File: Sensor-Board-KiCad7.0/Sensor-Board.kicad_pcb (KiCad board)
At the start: 2 copper layers, 75.4 x 75.4 mm, 128 parts, among them J2 B04B-XASK-1, U1 OPA396DCKT, U10 BME680, U11 OPA396DCKT, U12 OPA396DCKT, U14 OPA396DCKT, U15 MMBFJ177LT1, U16 MMBFJ177LT1, U17 MMBFJ177LT1, U18 NAU7802SGI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

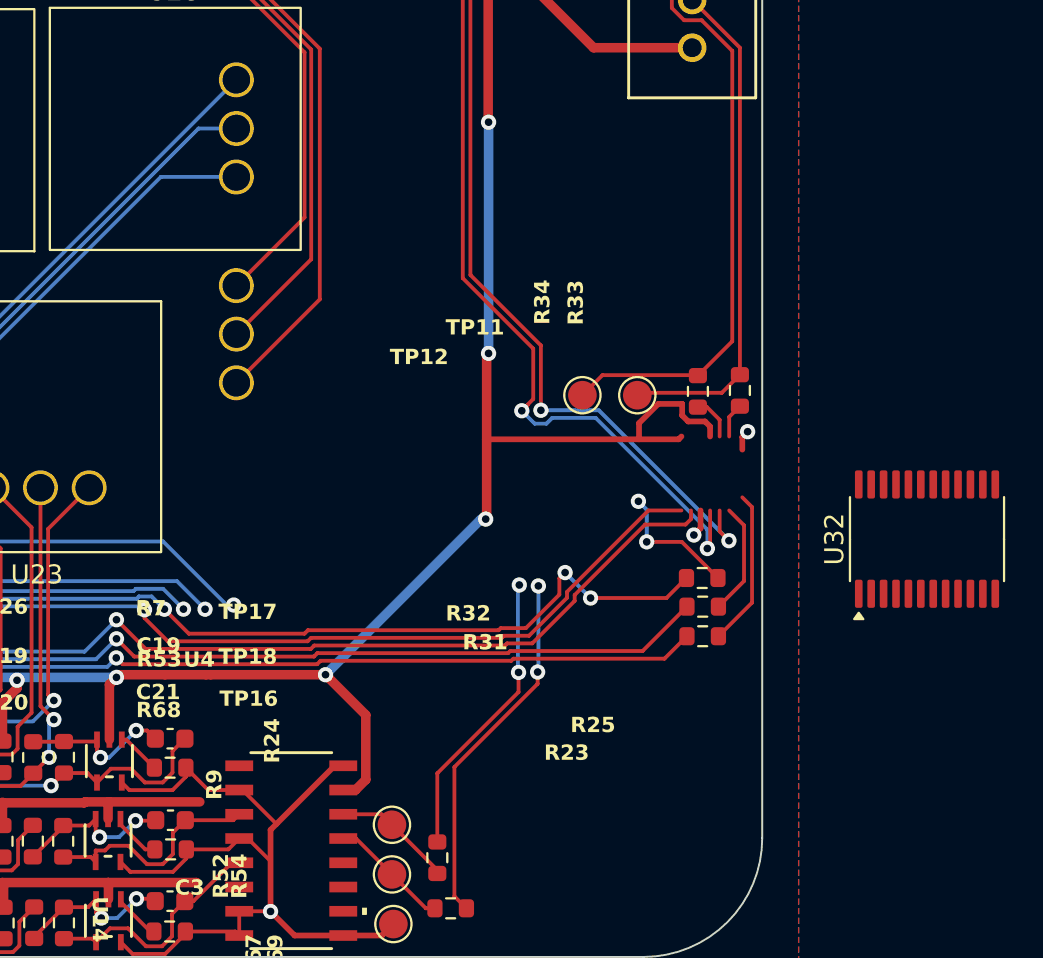
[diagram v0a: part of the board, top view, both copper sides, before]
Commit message: Moved resistors and wired the last of it all up
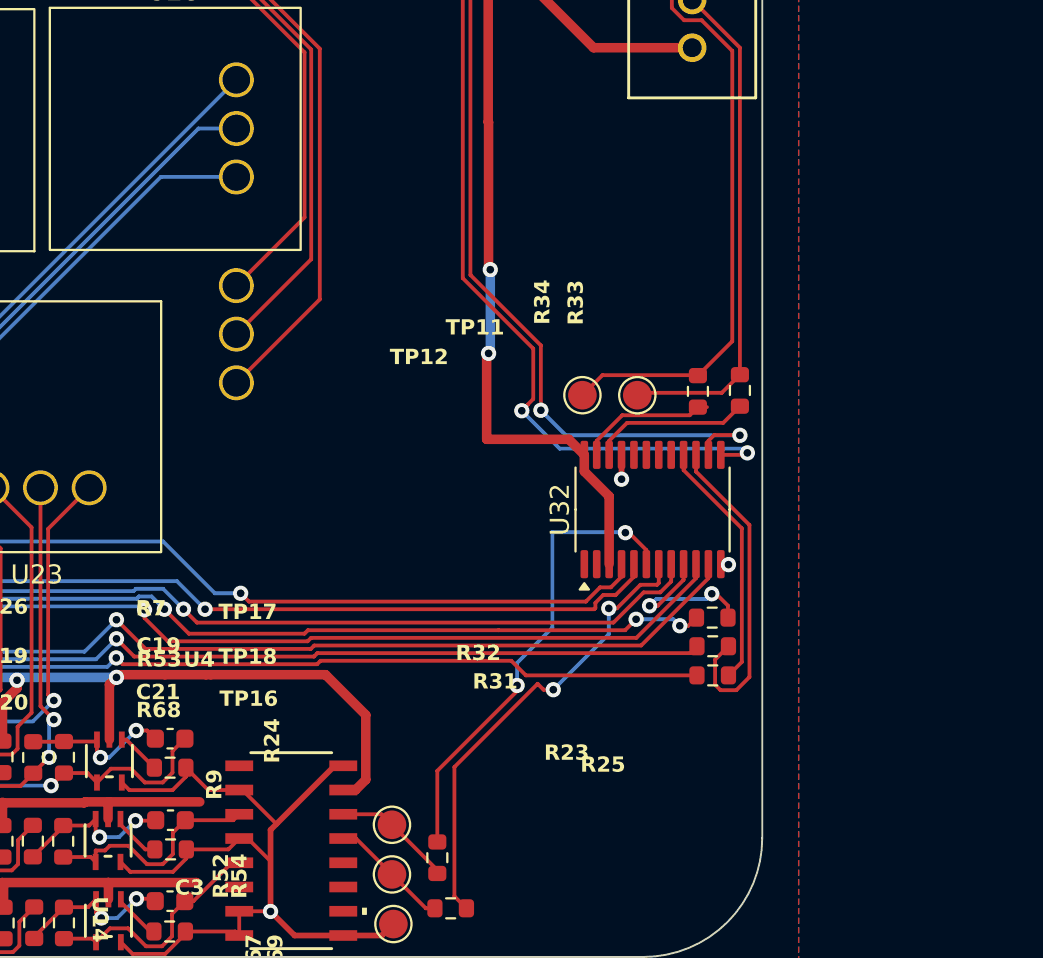
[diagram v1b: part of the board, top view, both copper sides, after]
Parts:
- moved U32 14.5 mm to (169.7, 109.9)
- moved R25 2.14 mm to (172.8, 115.5)
- moved R32 2.14 mm to (172.8, 117.0)
- moved R31 2.12 mm to (172.8, 118.6)
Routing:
- net Net-(U32-SD2): track 59.8 -> 87.4 mm
- net Net-(U32-SC0): track 59.2 -> 83.2 mm
- net Net-(U32-SD0): track 55.4 -> 76.8 mm
- net +3.3V: track 482.2 -> 461.4 mm, vias 15 -> 13
- net Net-(U32-SD5): track 5.91 -> 17.3 mm
- net Net-(U32-SD1): track 15.3 -> 24.8 mm
- net Net-(U32-SCL): track 1.82 -> 8.34 mm
- net Net-(U32-SC1): track 19.0 -> 24.4 mm
- net Net-(U32-SDA): track 2.29 -> 7.24 mm
- net Net-(U32-SC5): track 8.22 -> 13.1 mm
- net 680_SCL1: track 134.1 -> 132.4 mm
- net Net-(U32-SC2): track 6.82 -> 8.42 mm
- net Net-(U32-SC4): track 59.3 -> 58.3 mm
- net Net-(U32-SD4): track 61.2 -> 60.2 mm
- net GND: track 150.6 -> 149.8 mm

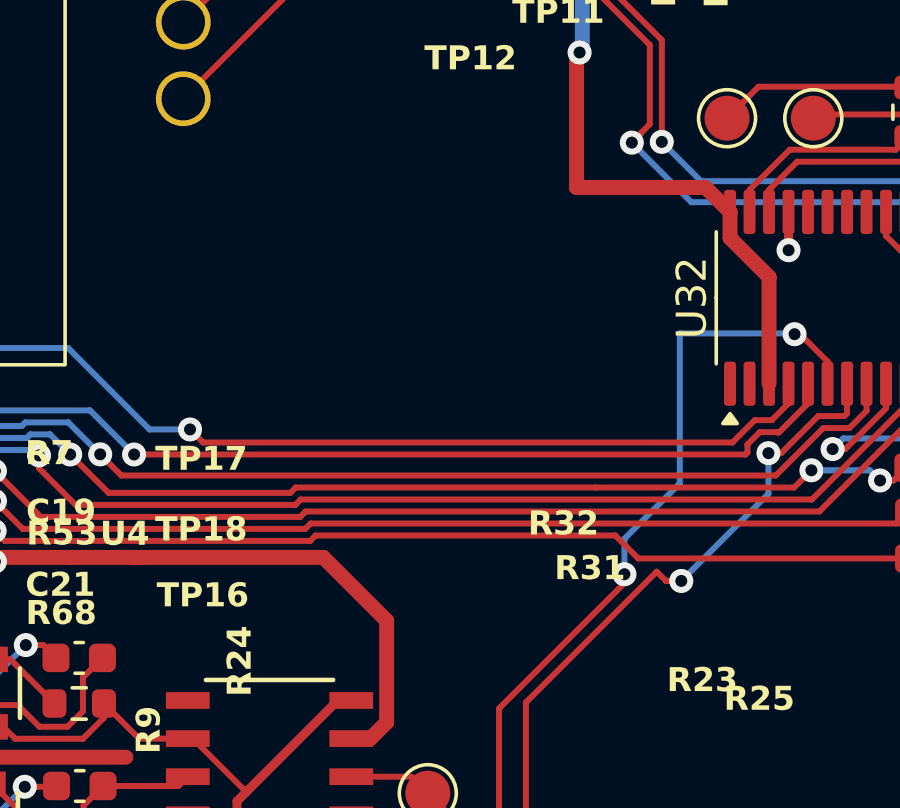
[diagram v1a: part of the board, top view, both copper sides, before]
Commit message: Rewired 3.3V to source line
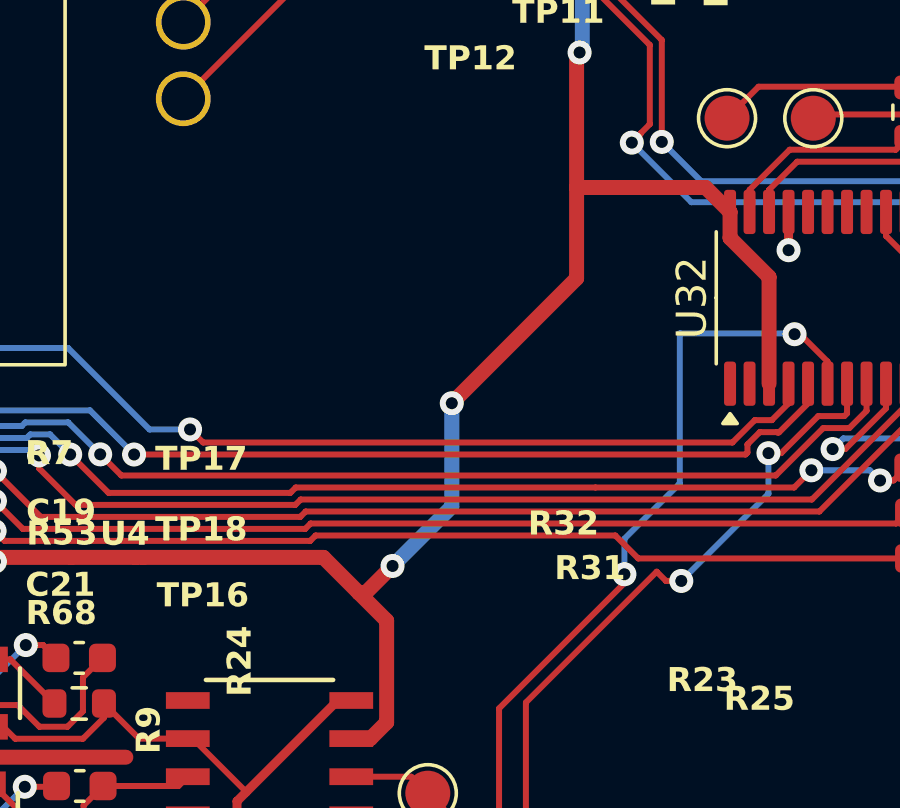
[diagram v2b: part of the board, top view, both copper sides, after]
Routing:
- net +3.3V: track 461.4 -> 478.1 mm, vias 13 -> 15
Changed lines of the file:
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@@
   (segment (start 122.32 100.772284) (end 121.845216 100.2975) (width 0.3) (layer "F.Cu") (net 9))
   (segment (start 122.649986 61.743336) (end 122.67 61.76335) (width 0.5) (layer "F.Cu") (net 9))
+  (segment (start 154.62855 120.64855) (end 153.7025 119.7225) (width 0.5) (layer "F.Cu") (net 9))
+  (segment (start 160.96 109.24) (end 156.8 113.4) (width 0.5) (layer "F.Cu") (net 9))
   (segment (start 122.77 65.84) (end 122.75 65.82) (width 0.5) (layer "F.Cu") (net 9))
   (segment (start 135.6 120.009188) (end 136.36 119.249188) (width 0.5) (layer "F.Cu") (net 9))
@@
   (segment (start 114.49 107.68) (end 114.49 105.52) (width 0.5) (layer "F.Cu") (net 9))
   (segment (start 103.92 81.85) (end 103.92 81.21035) (width 0.5) (layer "F.Cu") (net 9))
+  (segment (start 154.825 118.825) (end 153.9275 119.7225) (width 0.5) (layer "F.Cu") (net 9))
   (segment (start 136.36 119.249188) (end 136.36 118.83) (width 0.5) (layer "F.Cu") (net 9))
   (segment (start 103.92 84.062182) (end 103.682182 84.3) (width 0.5) (layer "F.Cu") (net 9))
@@
   (segment (start 154.08795 124.58) (end 154.62855 124.0394) (width 0.5) (layer "F.Cu") (net 9))
   (segment (start 117.28 123.37) (end 121.98 118.67) (width 0.5) (layer "F.Cu") (net 9))
+  (segment (start 153.9275 119.7225) (end 153.7025 119.7225) (width 0.5) (layer "F.Cu") (net 9))
   (segment (start 146.38 69.26) (end 146.38 71.6) (width 0.5) (layer "F.Cu") (net 9))
   (segment (start 120.71978 129.98) (end 117.44 129.98) (width 0.5) (layer "F.Cu") (net 9))
@@
   (segment (start 122.630001 129.356651) (end 122.630001 128.4979) (width 0.5) (layer "F.Cu") (net 9))
   (segment (start 111.20035 107.68) (end 114.49 107.68) (width 0.5) (layer "F.Cu") (net 9))
+  (segment (start 153.7025 119.7225) (end 152.52 118.54) (width 0.5) (layer "F.Cu") (net 9))
   (segment (start 116.51 70.1) (end 122.40545 70.1) (width 0.5) (layer "F.Cu") (net 9))
   (segment (start 135.55 65.78) (end 135.61 65.78) (width 0.5) (layer "F.Cu") (net 9))
@@
   (segment (start 120.72 100.91) (end 115.75 100.91) (width 0.3) (layer "F.Cu") (net 9))
   (segment (start 160.96 101.81) (end 160.96 106.21) (width 0.5) (layer "F.Cu") (net 9))
-  (segment (start 154.62855 120.64855) (end 152.52 118.54) (width 0.5) (layer "F.Cu") (net 9))
   (segment (start 161.06 89.6) (end 161.06 97.235) (width 0.5) (layer "F.Cu") (net 9))
   (segment (start 108.65 110.828668) (end 108.998418 110.48025) (width 0.5) (layer "F.Cu") (net 9))
   (segment (start 114.34 110.14) (end 114.49 109.99) (width 0.5) (layer "F.Cu") (net 9))
   (segment (start 121.52 100.2775) (end 121.5 100.2975) (width 0.3) (layer "F.Cu") (net 9))
+  (segment (start 160.96 106.21) (end 160.96 109.24) (width 0.5) (layer "F.Cu") (net 9))
   (segment (start 122.649986 60.8879) (end 122.649986 61.743336) (width 0.5) (layer "F.Cu") (net 9))
   (segment (start 102.925 100.35) (end 112.61 100.35) (width 0.5) (layer "F.Cu") (net 9))
@@
   (via (at 114.35 80.38) (size 0.8) (drill 0.4) (layers "F.Cu" "B.Cu") (net 9))
   (via (at 161.225 80.365) (size 0.8) (drill 0.4) (layers "F.Cu" "B.Cu") (net 9))
+  (via (at 156.8 113.4) (size 0.8) (drill 0.4) (layers "F.Cu" "B.Cu") (net 9))
+  (via (at 154.825 118.825) (size 0.8) (drill 0.4) (layers "F.Cu" "B.Cu") (net 9))
   (via (at 136.36 118.83) (size 0.8) (drill 0.4) (layers "F.Cu" "B.Cu") (net 9))
   (via (at 161.06 101.71) (size 0.8) (drill 0.4) (layers "F.Cu" "B.Cu") (net 9))
@@
   (segment (start 122.21 93.3) (end 122.21 91.65) (width 0.3) (layer "B.Cu") (net 9))
   (segment (start 114.34 111.03) (end 121.98 118.67) (width 0.5) (layer "B.Cu") (net 9))
+  (segment (start 156.8 113.4) (end 156.8 116.85) (width 0.5) (layer "B.Cu") (net 9))
+  (segment (start 156.8 116.85) (end 154.825 118.825) (width 0.5) (layer "B.Cu") (net 9))
   (segment (start 122.17 72.5) (end 122.17 72.43) (width 0.5) (layer "B.Cu") (net 9))
   (segment (start 122.647499 93.4) (end 122.31 93.4) (width 0.3) (layer "B.Cu") (net 9))

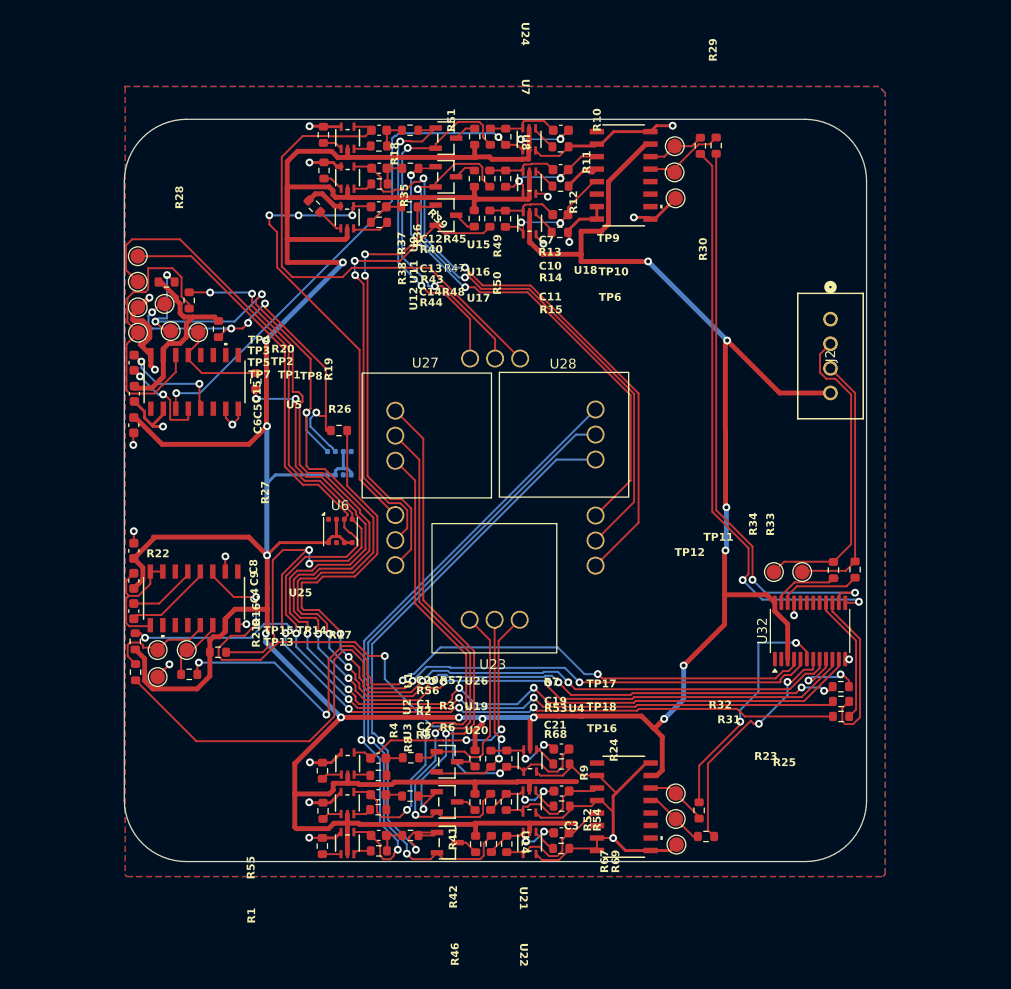
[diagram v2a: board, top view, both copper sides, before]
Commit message: Ordered silk screen stuff around circuit and wired up some unwired grnds
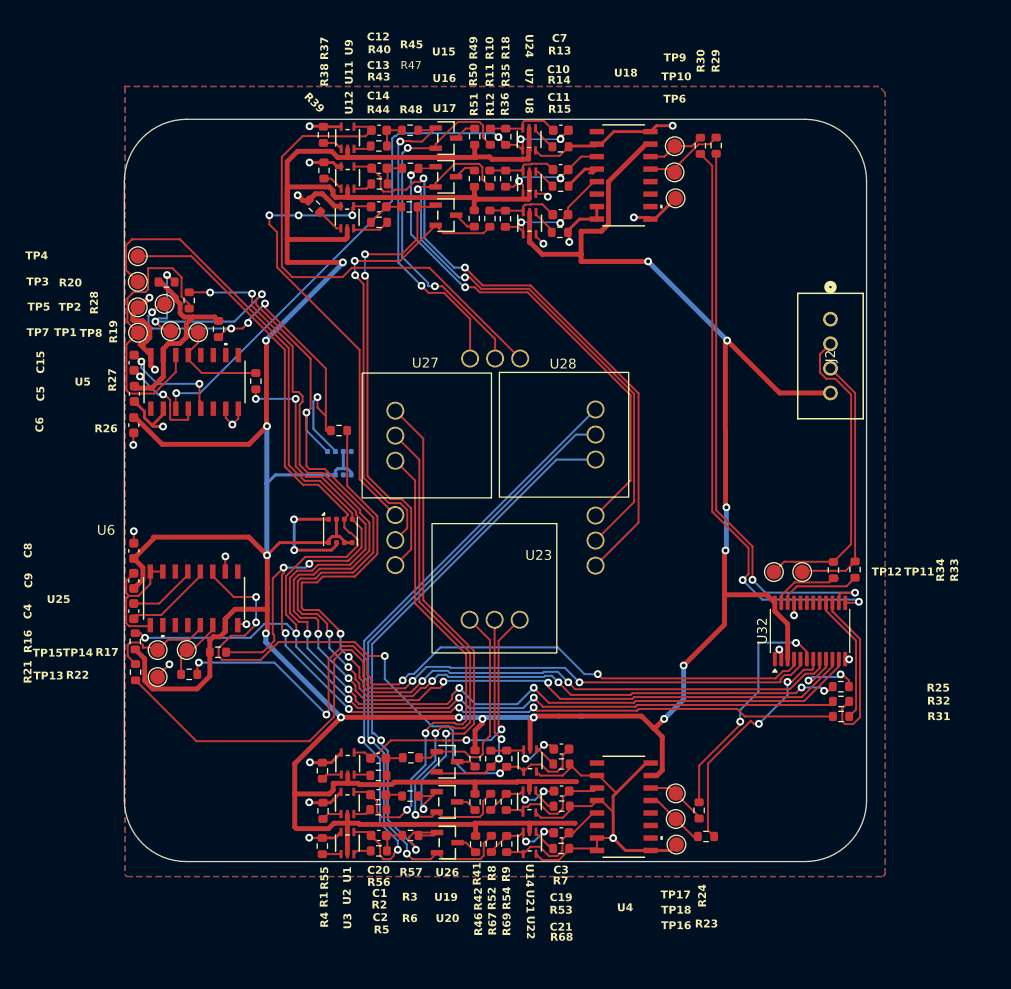
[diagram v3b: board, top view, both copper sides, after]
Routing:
- net GND: track 149.8 -> 163.6 mm, vias 22 -> 26
- net 680_SCL2: track 145.8 -> 139.8 mm
- net 680_SDA1: track 40.3 -> 42.8 mm

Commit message: Updated board edge clearance settings
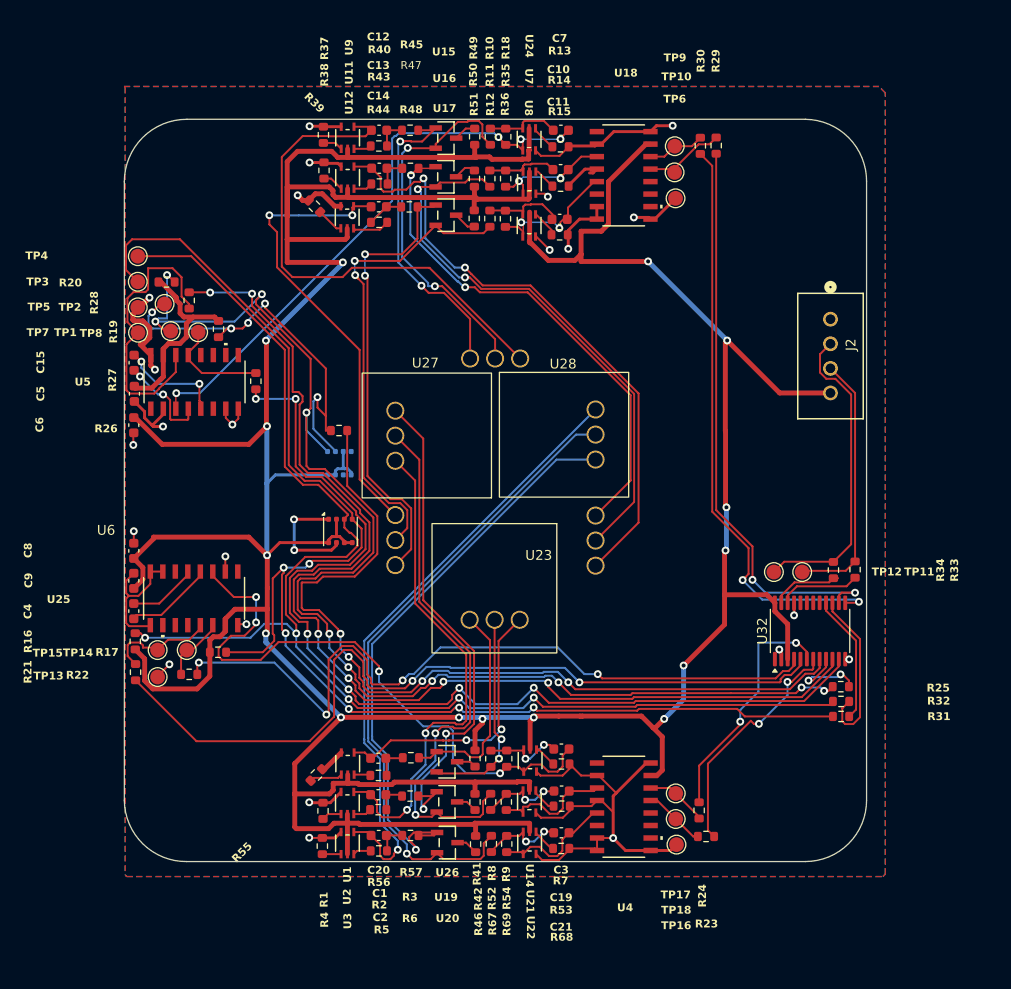
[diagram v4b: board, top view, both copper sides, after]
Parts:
- moved R55 0.75 mm to (119.5, 124.5), turned to 45 degrees
- moved C11 0.48 mm to (144.2, 68.0)
- moved R15 0.25 mm to (144.2, 69.6)
- moved U8 0.24 mm to (141.1, 68.7)
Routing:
- net +3.3V: track 478.1 -> 469.1 mm
- net Sens2_CO: track 60.3 -> 58.0 mm
- net Net-(U1-+IN): track 2.10 -> 3.37 mm
- net GND: track 163.6 -> 162.7 mm, vias 26 -> 25
- net AOut2_SO2: track 13.6 -> 14.2 mm
- net Count1_SO2: track 63.0 -> 62.7 mm, vias 2 -> 1
- net Ref1_SO2: track 60.0 -> 59.8 mm, vias 2 -> 1
- net Sens1_SO2: vias 2 -> 1
- net Count2_SO2: vias 3 -> 2

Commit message: Fixing Violations
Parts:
- moved TP4 0.73 mm to (102.0, 71.6)
- moved R20 0.56 mm to (104.2, 73.9)
- moved R27 0.39 mm to (113.7, 84.4)
- moved TP5 0.39 mm to (101.7, 76.9)
- moved TP2 0.30 mm to (104.3, 76.7)
- moved R28 0.22 mm to (106.8, 76.2)
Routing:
- net GND: track 162.7 -> 177.6 mm, vias 25 -> 30
- net +3.3V: track 469.1 -> 455.5 mm
- net ADC3_SDA: track 30.0 -> 38.8 mm, vias 0 -> 4
- net Count1_SO2: track 62.7 -> 56.1 mm
- net Ref2_CO: track 51.5 -> 45.4 mm
- net ADC4_SCL: track 8.52 -> 11.6 mm, vias 0 -> 2
- net Sens2_NO2: track 37.9 -> 35.2 mm
- net ADC1_SCL: track 11.5 -> 10.0 mm, vias 0 -> 2
- net Sens1_SO2: track 66.0 -> 64.6 mm, vias 1 -> 3
- net 680_SDA1: track 42.8 -> 43.9 mm
- net 680_SCL1: track 132.4 -> 133.4 mm
- net Ref2_NO2: track 32.2 -> 31.2 mm
- net AOut2_SO2: track 14.2 -> 14.8 mm
- net 680_SDA2: track 135.9 -> 135.3 mm
- net Net-(U32-SD3): track 115.7 -> 115.1 mm
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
